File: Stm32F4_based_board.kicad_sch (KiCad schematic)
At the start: 50 parts, among them J1 Screw_Terminal_01x02, J2 SWD, J3 I2C1, J4 USART3, J5 USB_B_Micro, Q1 AO3401A, SW1 SW_SPDT, U1 STM32F405RGT6, U3 USBLC6-2SC6, Y1 16MHz

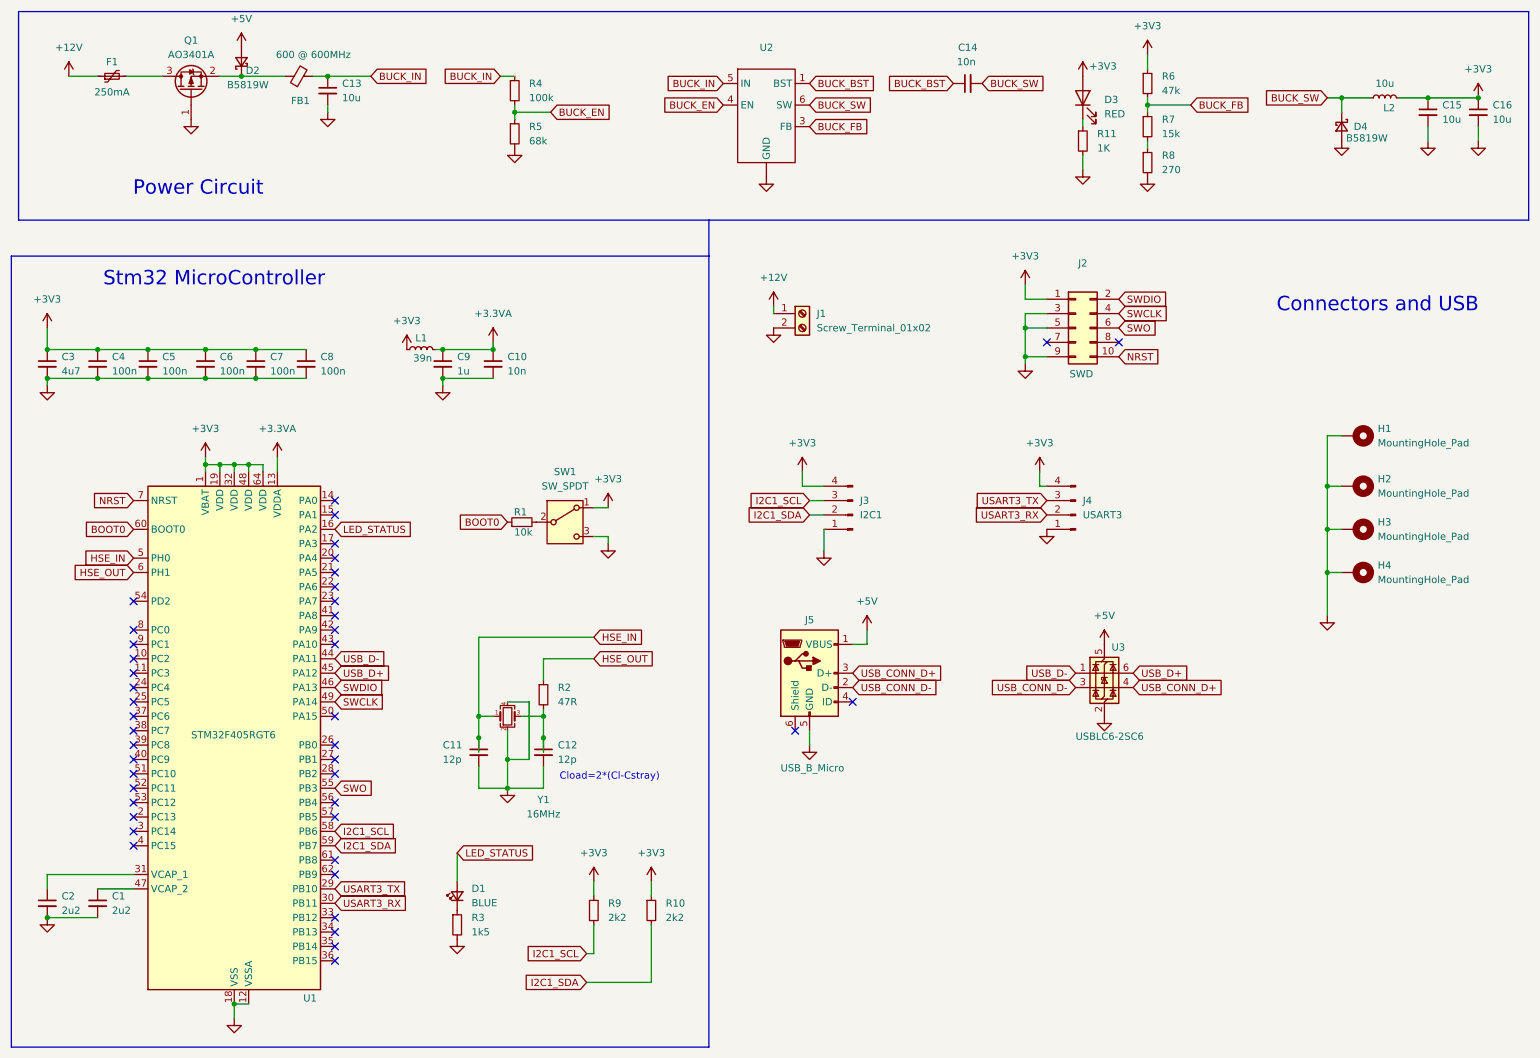
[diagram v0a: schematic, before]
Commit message: updated into PCB with the usb 3d model
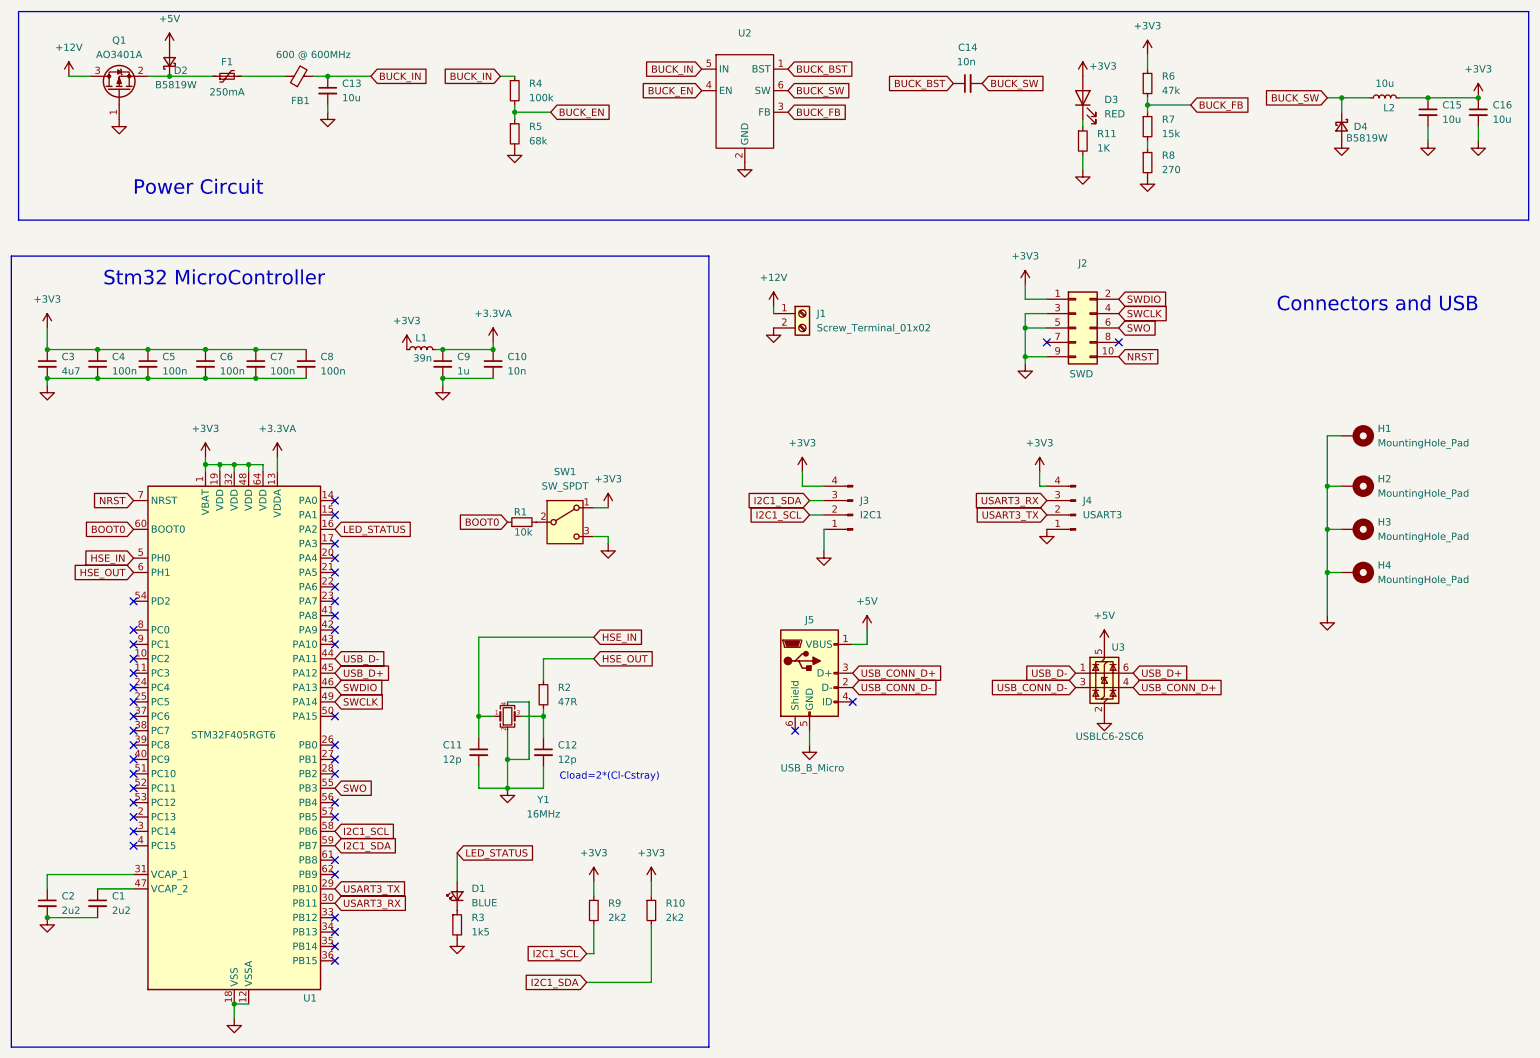
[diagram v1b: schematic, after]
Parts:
- J4: footprint Connector_USB:USB_Micro-B_Wuerth_629105150521 -> Connector_Molex:Molex_PicoBlade_53048-0410_1x04_P1.25mm_Horizontal
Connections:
- net +12V: now also Q1.3 (D); no longer F1.1
- net GND: now also U2.2 (GND); no longer U2. (GND)
- net I2C1_SCL: now also J3.2 (Pin_2); no longer J3.3 (Pin_3)
- net I2C1_SDA: now also J3.3 (Pin_3); no longer J3.2 (Pin_2)
- net USART3_RX: now also J4.3 (Pin_3); no longer J4.2 (Pin_2)
- net USART3_TX: now also J4.2 (Pin_2); no longer J4.3 (Pin_3)
- net at F1.2: now also FB1.1; no longer Q1.3 (D)
- net at D2.1 (K), Q1.2 (S): now also F1.1; no longer FB1.1
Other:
- moved on the sheet: D2, F1, Q1
